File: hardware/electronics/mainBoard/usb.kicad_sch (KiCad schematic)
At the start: 2 parts, among them J1 USB_C_Receptacle_USB2.0, U2 TPS25730D

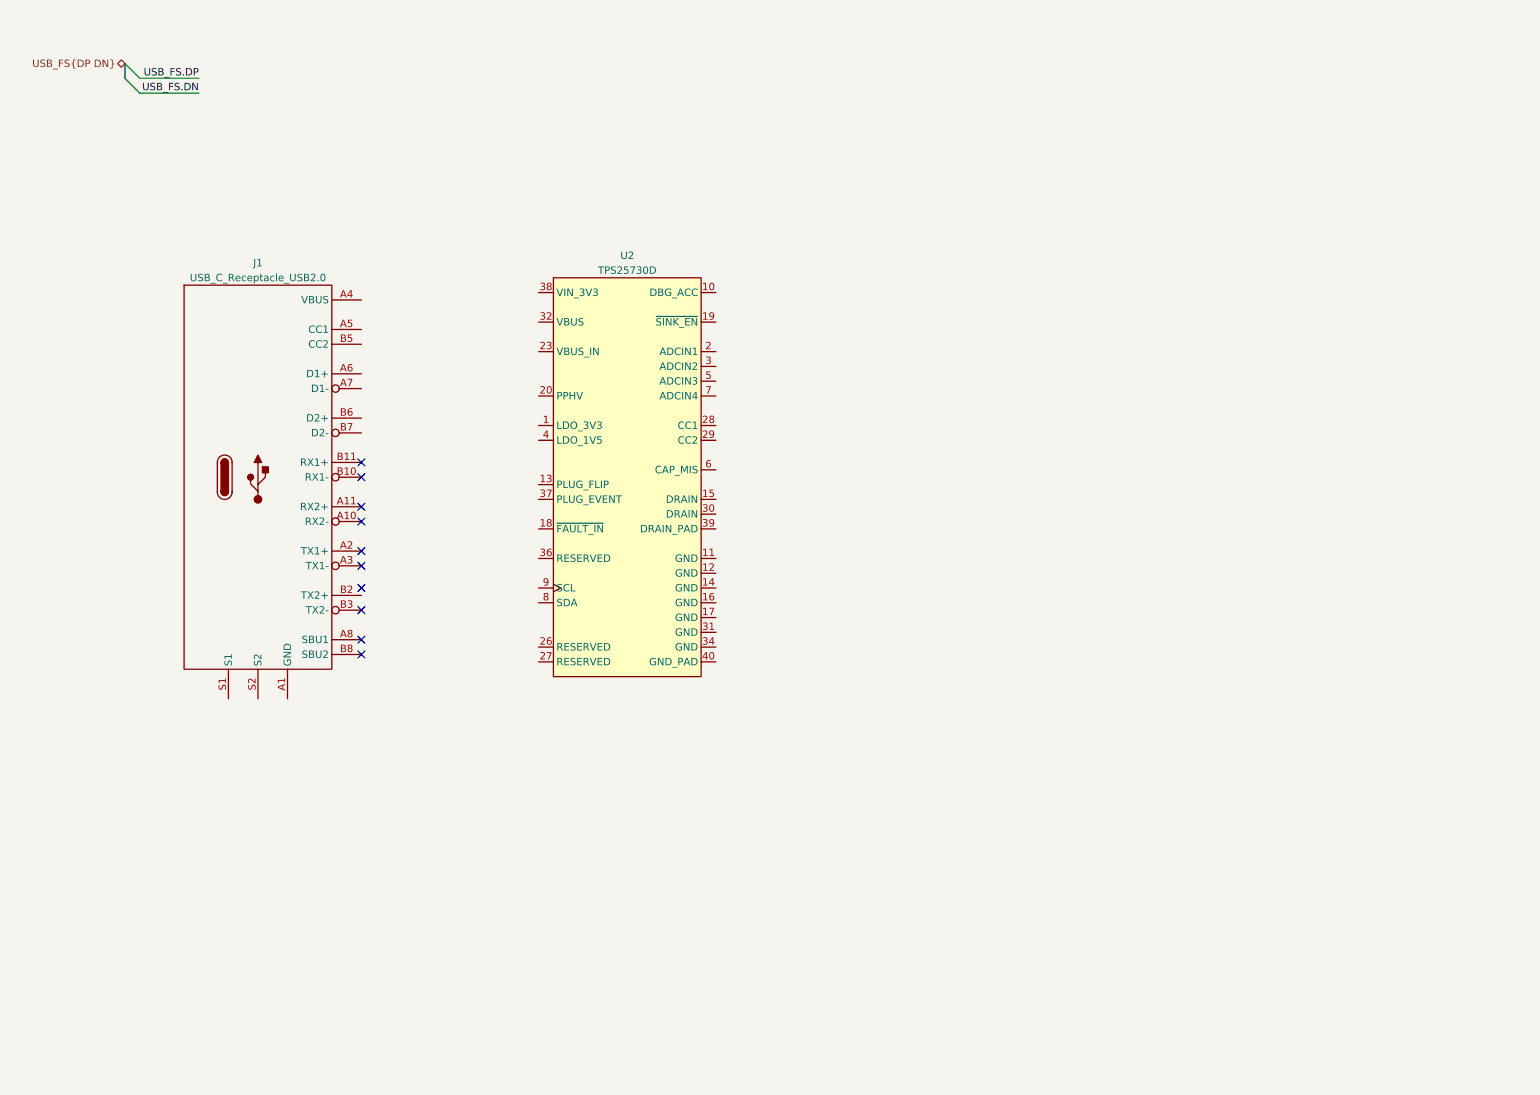
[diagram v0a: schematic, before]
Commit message: added USB PD and Hub circuitry
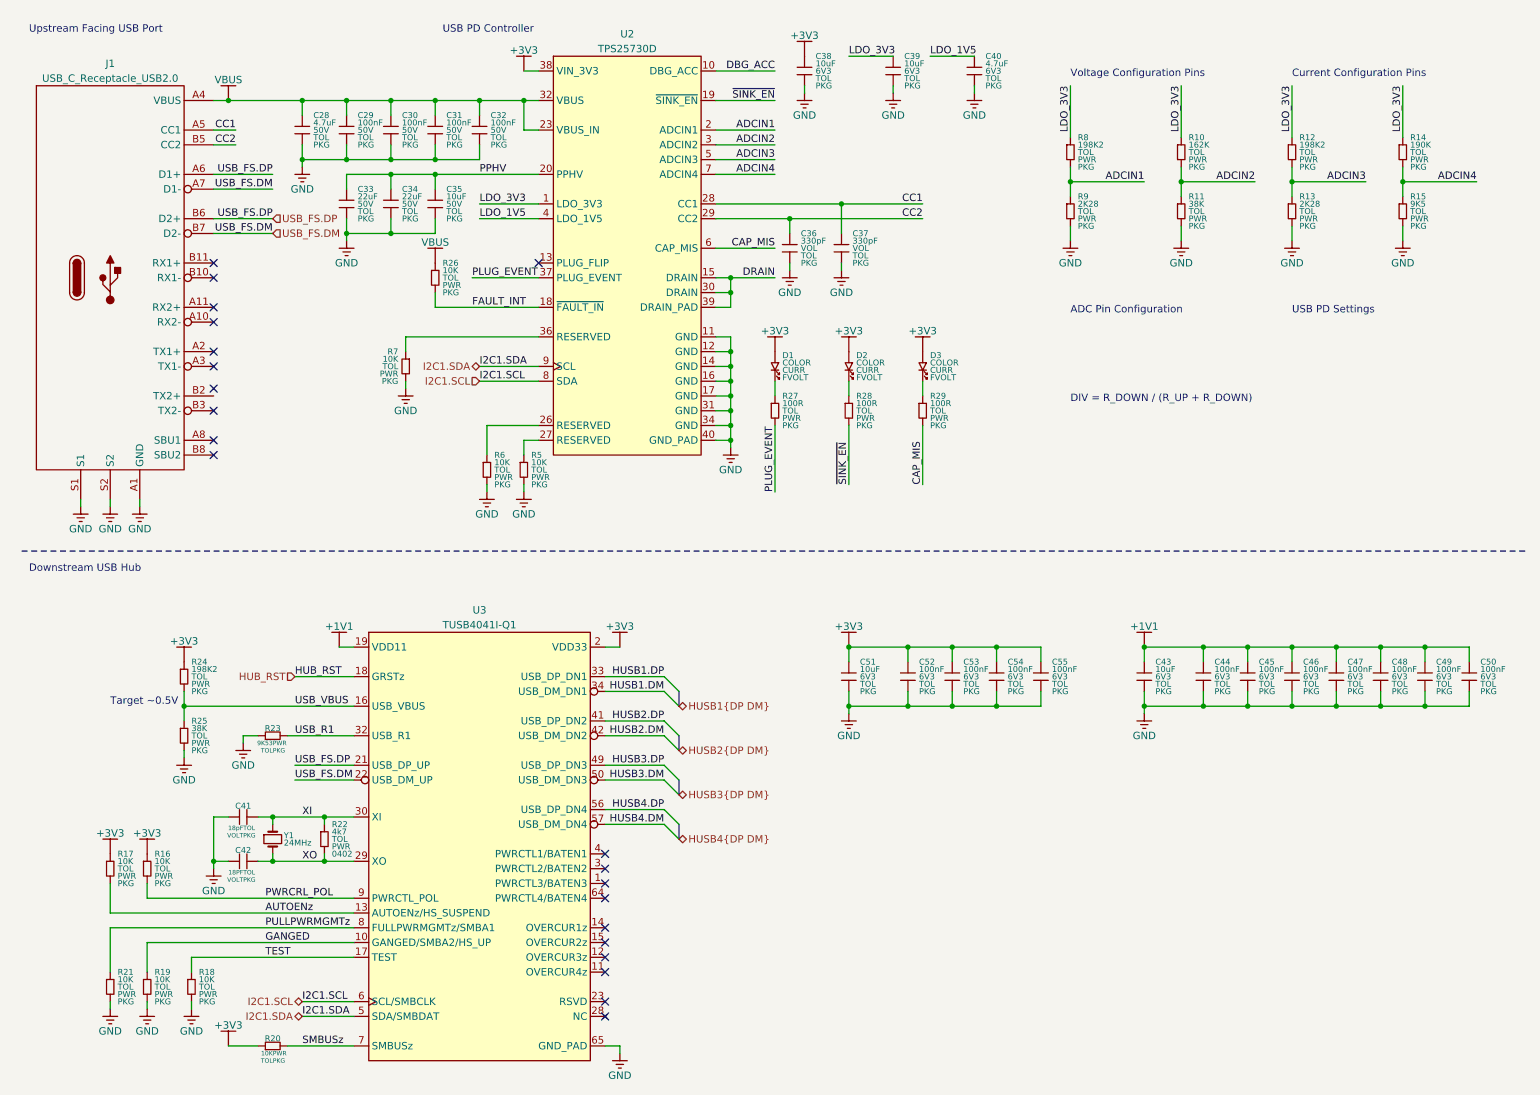
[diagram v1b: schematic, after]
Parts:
- added C28, C40: 4.7uF, symbol .DS-Passives:C
- added C29, C30, C31, C32, C44, C45, C46, C47, C48, C49, C50, C52, C53, C54, C55: 100nF, symbol .DS-Passives:C
- added C33, C34: 22uF, symbol .DS-Passives:C
- added C35, C38, C39, C43, C51: 10uF, symbol .DS-Passives:C
- added C36, C37: 330pF, symbol .DS-Passives:C
- added C41: 18pF, symbol .DS-Passives:C_horizontal
- added C42: 18PF, symbol .DS-Passives:C_horizontal
- added D1, D2, D3: ~, symbol .DS-LEDs:LED
- added R10: 162K, symbol .DS-Passives:R
- added R11, R25: 38K, symbol .DS-Passives:R
- added R12, R24, R8: 198K2, symbol .DS-Passives:R
- added R13, R9: 2K28, symbol .DS-Passives:R
- added R14: 190K, symbol .DS-Passives:R
- added R15: 9K5, symbol .DS-Passives:R
- added R16, R17, R18, R19, R21, R26, R5, R6, R7: 10K, symbol .DS-Passives:R
- added R20: 10K, symbol .DS-Passives:R_horizontal
- added R22: 4k7, symbol .DS-Passives:R
- added R23: 9K53, symbol .DS-Passives:R_horizontal
- added R27, R28, R29: 100R, symbol .DS-Passives:R
- added U3: TUSB4041I-Q1, symbol .DS-ICs:TUSB4041I-Q1
- added Y1: ~, symbol .DS-Crystals-Oscillators-Resonators:crystal_small
- U2: DKPN (none) -> 296-TPS25730DREFRCT-ND; MPN (none) -> TPS25730DREFR
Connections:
- net USB_FS.DP: now also J1.A6 (D1+), J1.B6 (D2+), U3.21 (USB_DP_UP)
- net GND: now reaches J1.A1 (GND), J1.A12 (GND), J1.B1 (GND), J1.B12 (GND)
- net GND: now also J1.S1, J1.S2, U2.11 (GND), U2.12 (GND), U2.14 (GND), U2.16 (GND), U2.17 (GND), U2.31 (GND), U2.34 (GND), U2.35 (GND), U2.40 (GND_PAD), C28.2, C29.2, C30.2, C31.2, C32.2, C33.2, C34.2, C35.2, C36.2, C37.2, C38.2, C39.2, C40.2, C41.1, C42.1, C43.2, C44.2, C45.2, C46.2, C47.2, C48.2, C49.2, C50.2, C51.2, C52.2, C53.2, C54.2, C55.2, R11.2, R13.2, R15.2, R18.2, R19.2, R21.2, R23.1, R25.2, R5.2, R6.2, R7.2, R9.2, U3.65 (GND_PAD)
- net VBUS: now reaches J1.A4 (VBUS), J1.A9 (VBUS), J1.B4 (VBUS), J1.B9 (VBUS)
- net VBUS: now also U2.23 (VBUS_IN), U2.24 (VBUS_IN), U2.25 (VBUS_IN), U2.32 (VBUS), U2.33 (VBUS), C28.1, C29.1, C30.1, C31.1, C32.1, R26.1
- net CC1: now reaches J1.A5 (CC1)
- net CC1: now also U2.28 (CC1), C37.1
- net USB_FS.DM: now reaches J1.A7 (D1-)
- net USB_FS.DM: now also J1.B7 (D2-), U3.22 (USB_DM_UP)
- net CC2: now reaches J1.B5 (CC2)
- net CC2: now also U2.29 (CC2), C36.1
- net LDO_3V3: now reaches U2.1 (LDO_3V3)
- net LDO_3V3: now also C39.1, R10.1, R12.1, R14.1, R8.1
- net DBG_ACC: now reaches U2.10 (DBG_ACC)
- net DRAIN: now reaches U2.15 (DRAIN)
- net DRAIN: now also U2.30 (DRAIN), U2.39 (DRAIN_PAD)
- net FAULT_INT: now reaches U2.18 (~{FAULT_IN})
- net FAULT_INT: now also R26.2
- net ~{SINK_EN}: now reaches U2.19 (~{SINK_EN})
- net ~{SINK_EN}: now also R28.2
- net ADCIN1: now reaches U2.2 (ADCIN1)
- net ADCIN1: now also R8.2, R9.1
- net PPHV: now reaches U2.20 (PPHV), U2.21 (PPHV), U2.22 (PPHV)
- net PPHV: now also C33.1, C34.1, C35.1
- net at U2.26 (RESERVED): now also R6.1
- net at U2.27 (RESERVED): now also R5.1
- net ADCIN2: now reaches U2.3 (ADCIN2)
- net ADCIN2: now also R10.2, R11.1
- net at U2.36 (RESERVED): now also R7.1
- net PLUG_EVENT: now reaches U2.37 (PLUG_EVENT)
- net PLUG_EVENT: now also R27.2
- net +3V3: now reaches U2.38 (VIN_3V3)
- net +3V3: now also C38.1, C51.1, C52.1, C53.1, C54.1, C55.1, D1.1, D2.1, D3.1, R16.1, R17.1, R20.1, R24.1, U3.2 (VDD33), U3.20 (VDD33), U3.31 (VDD33), U3.48 (VDD33)
- net LDO_1V5: now reaches U2.4 (LDO_1V5)
- net LDO_1V5: now also C40.1
- net ADCIN3: now reaches U2.5 (ADCIN3)
- net ADCIN3: now also R12.2, R13.1
- net CAP_MIS: now reaches U2.6 (CAP_MIS)
- net CAP_MIS: now also R29.2
- net ADCIN4: now reaches U2.7 (ADCIN4)
- net ADCIN4: now also R14.2, R15.1
- net I2C1.SCL: now reaches U2.8 (SDA)
- net I2C1.SCL: now also U3.6 (SCL/SMBCLK)
- net I2C1.SDA: now reaches U2.9 (SCL)
- net I2C1.SDA: now also U3.5 (SDA/SMBDAT)
- new net: D2.2, R28.1
- new net: D1.2, R27.1
- new net: D3.2, R29.1
- new net: U3.23 (RSVD), U3.24 (RSVD), U3.26 (RSVD), U3.27 (RSVD), U3.35 (RSVD), U3.36 (RSVD), U3.38 (RSVD), U3.39 (RSVD), U3.43 (RSVD), U3.44 (RSVD), U3.46 (RSVD), U3.47 (RSVD), U3.51 (RSVD), U3.52 (RSVD), U3.54 (RSVD), U3.55 (RSVD), U3.58 (RSVD), U3.59 (RSVD), U3.61 (RSVD), U3.62 (RSVD)
- new net: U3.28 (NC), U3.40 (NC)
- new net +1V1: C43.1, C44.1, C45.1, C46.1, C47.1, C48.1, C49.1, C50.1, U3.19 (VDD11), U3.25 (VDD11), U3.37 (VDD11), U3.45 (VDD11), U3.53 (VDD11), U3.60 (VDD11), U3.63 (VDD11)
- new net AUTOENz: R17.2, U3.13 (AUTOENz/HS_SUSPEND)
- new net GANGED: R19.1, U3.10 (GANGED/SMBA2/HS_UP)
- new net HUB_RST: U3.18 (GRSTz)
- new net HUSB1.DM: U3.34 (USB_DM_DN1)
- new net HUSB1.DP: U3.33 (USB_DP_DN1)
- new net HUSB2.DM: U3.42 (USB_DM_DN2)
- new net HUSB2.DP: U3.41 (USB_DP_DN2)
- new net HUSB3.DM: U3.50 (USB_DM_DN3)
- new net HUSB3.DP: U3.49 (USB_DP_DN3)
- new net HUSB4.DM: U3.57 (USB_DM_DN4)
- new net HUSB4.DP: U3.56 (USB_DP_DN4)
- new net PULLPWRMGMTz: R21.1, U3.8 (FULLPWRMGMTz/SMBA1)
- new net PWRCRL_POL: R16.2, U3.9 (PWRCTL_POL)
- new net SMBUSz: R20.2, U3.7 (SMBUSz)
- new net TEST: R18.1, U3.17 (TEST)
- new net USB_R1: R23.2, U3.32 (USB_R1)
- new net USB_VBUS: R24.2, R25.1, U3.16 (USB_VBUS)
- new net XI: C41.2, R22.1, U3.30 (XI), Y1.1
- new net XO: C42.2, R22.2, U3.29 (XO), Y1.2
- no-connect marks 10 -> 21
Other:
- note added: "ADC Pin Configuration"
- note added: "Current Configuration Pins"
- note added: "DIV = R_DOWN / (R_UP + R_DOWN)"
- note added: "Downstream USB Hub"
- note added: "Target ~0.5V"
- note added: "USB PD Controller"
- note added: "USB PD Settings"
- note added: "Upstream Facing USB Port"
- note added: "Voltage Configuration Pins"
- moved on the sheet: J1, U2

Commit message: usb PD and hub
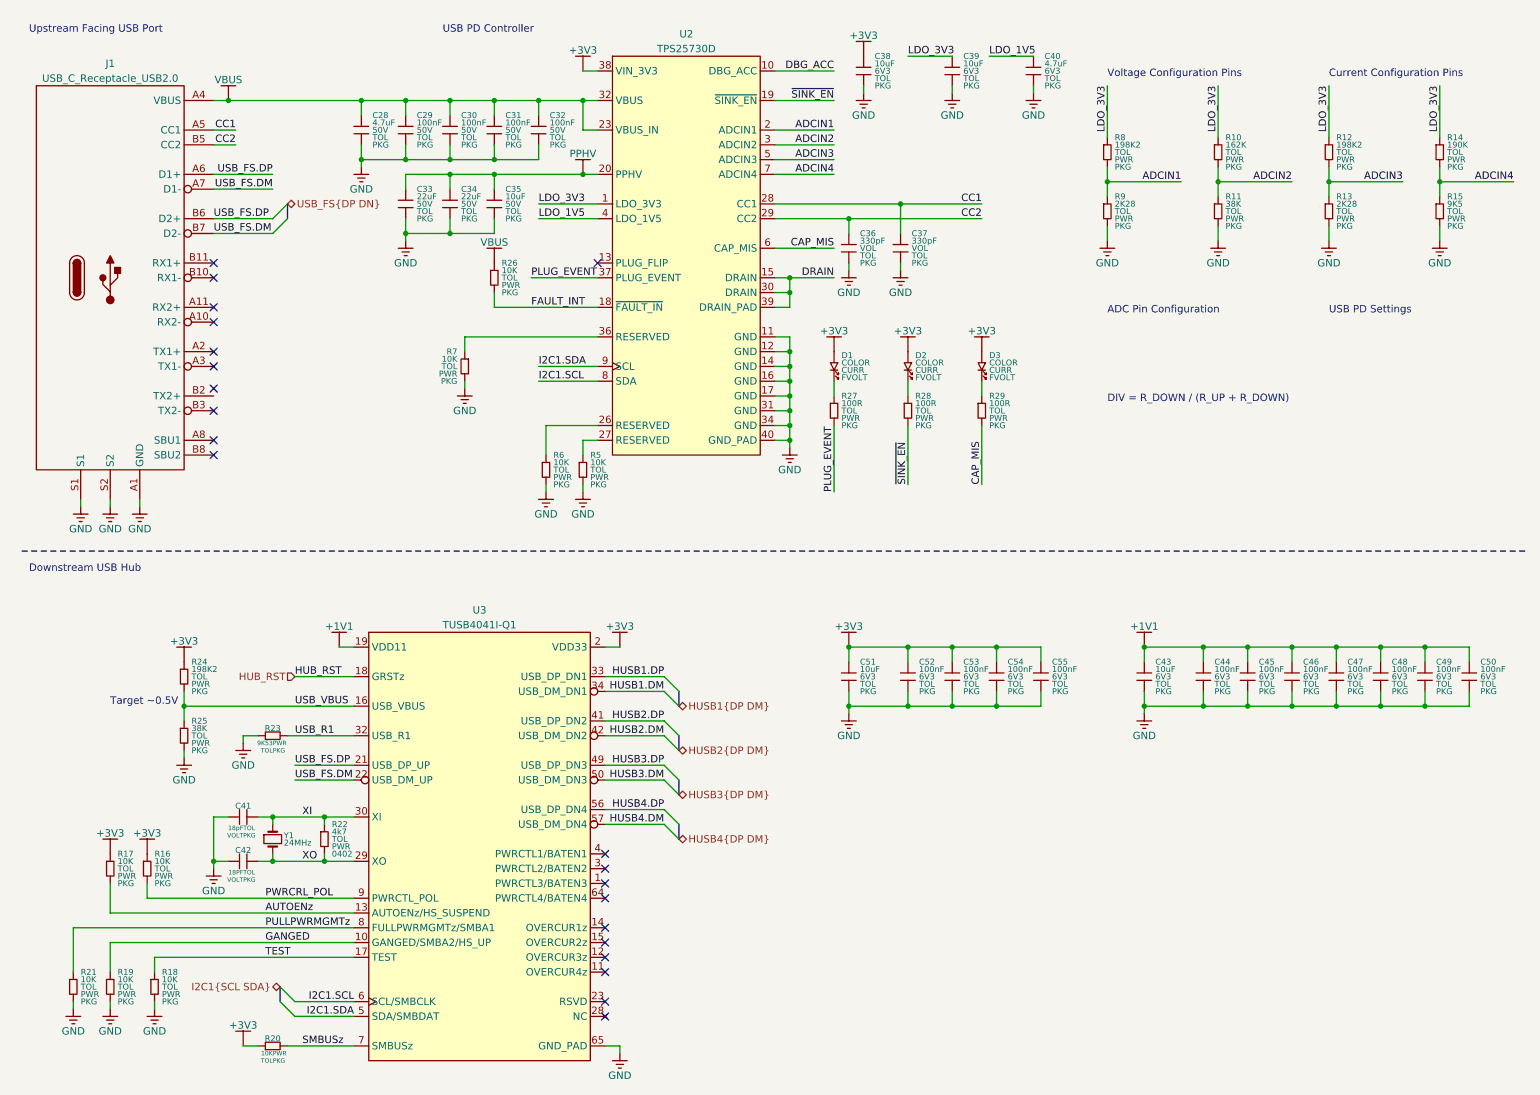
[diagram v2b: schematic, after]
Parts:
- C28, C29, C30, C31, C32, C33, C34, C35, C36, C37, C38, C39, C40, C43, C44, C45, C46, C47, C48, C49, C50, C51, C52, C53, C54, C55: symbol .DS-Passives:C -> lib_sch:C
- C41, C42: symbol .DS-Passives:C_horizontal -> lib_sch:C_horizontal
- D1, D2, D3: symbol .DS-LEDs:LED -> lib_sch:LED
- R10, R11, R12, R13, R14, R15, R16, R17, R18, R19, R21, R22, R24, R25, R26, R27, R28, R29, R5, R6, R7, R8, R9: symbol .DS-Passives:R -> lib_sch:R
- R20, R23: symbol .DS-Passives:R_horizontal -> lib_sch:R_horizontal
- U3: symbol .DS-ICs:TUSB4041I-Q1 -> lib_sch:TUSB4041I-Q1
- Y1: symbol .DS-Crystals-Oscillators-Resonators:crystal_small -> lib_sch:crystal_small
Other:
- moved on the sheet: C28, C29, C30, C31, C32, C33, C34, C35, C36, C37, C38, C39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

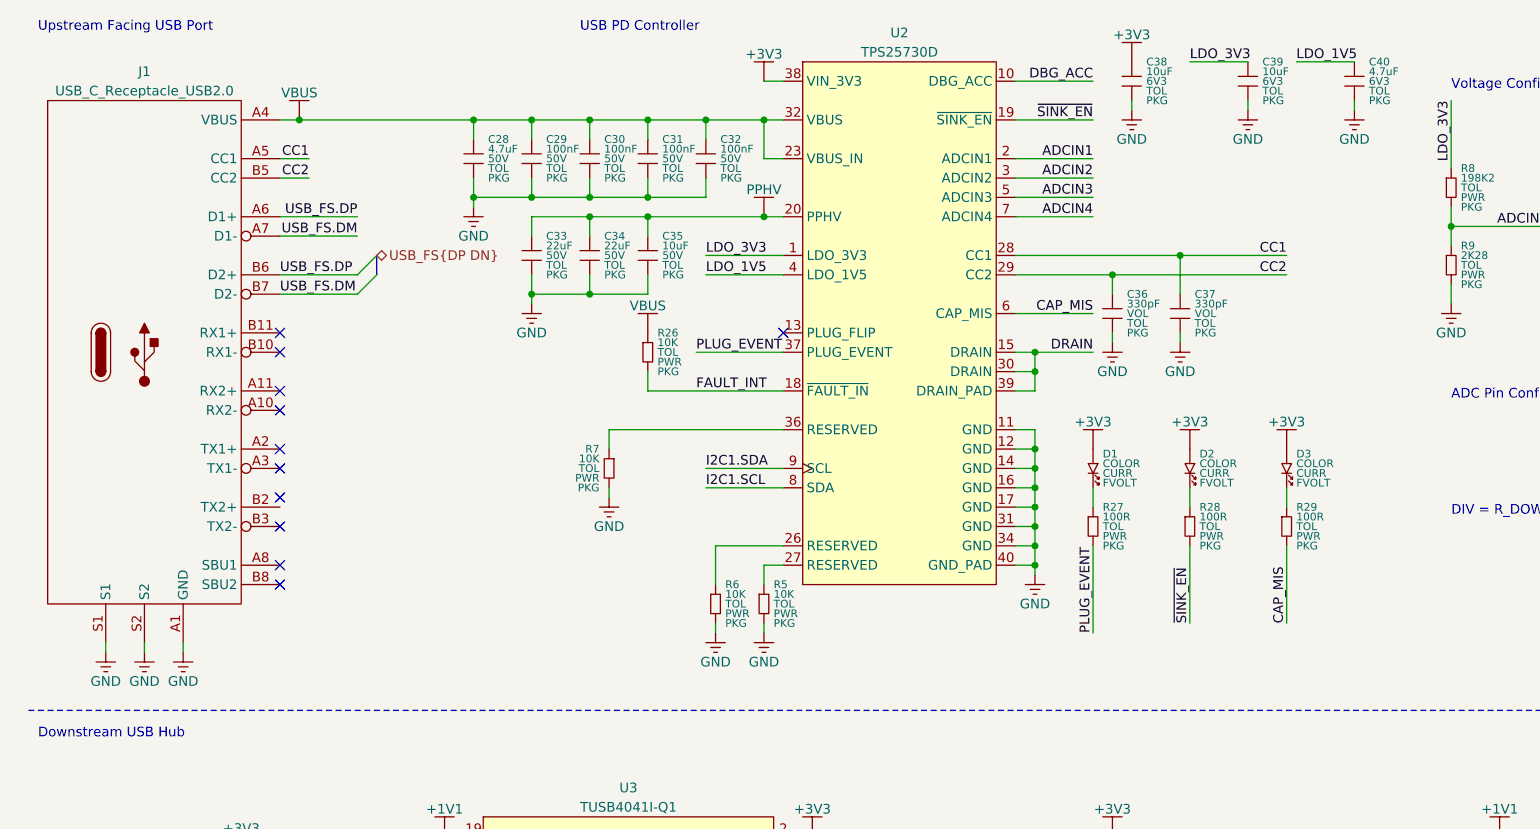
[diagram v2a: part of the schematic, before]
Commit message: replaced PD IC
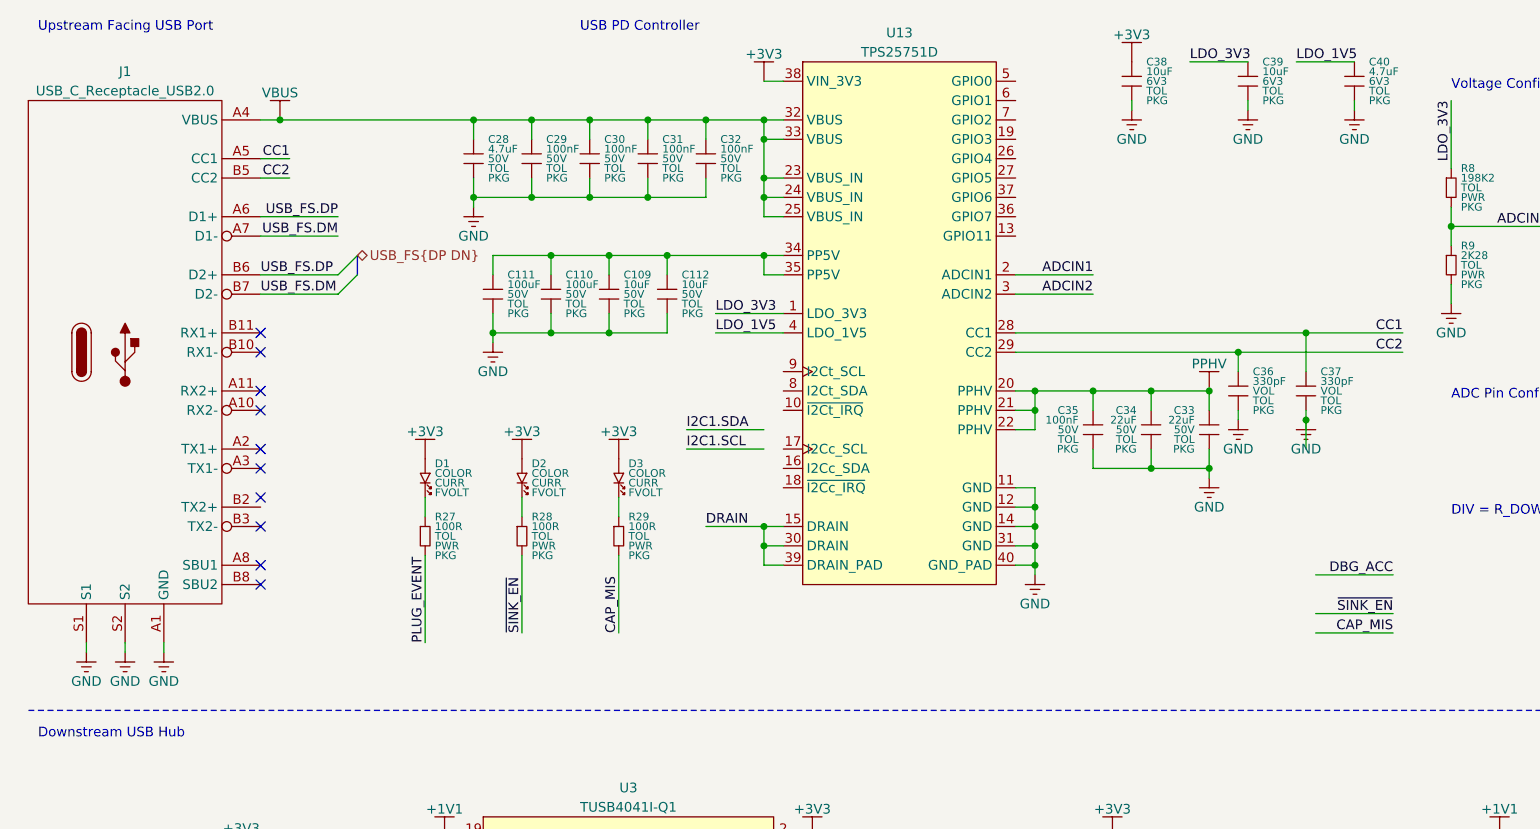
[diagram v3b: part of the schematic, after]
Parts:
- removed R26, R5, R6, R7: 10K, symbol lib_sch:R
- removed U2: TPS25730D, symbol lib_sch:TPS25730D
- added C109, C112: 10uF, symbol lib_sch:C
- added C110, C111: 100uF, symbol lib_sch:C
- added U13: TPS25751D, symbol .DS-PMIC:TPS25751D
- C35: value 10uF -> 100nF
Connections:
- net +3V3: now also U13.38 (VIN_3V3)
- net ADCIN1: now also U13.2 (ADCIN1)
- net ADCIN2: now also U13.3 (ADCIN2)
- net CC1: now also U13.28 (CC1)
- net CC2: now also U13.29 (CC2)
- net DRAIN: now also U13.15 (DRAIN), U13.30 (DRAIN), U13.39 (DRAIN_PAD)
- net GND: now also C109.2, C110.2, C111.2, C112.2, U13.11 (GND), U13.12 (GND), U13.14 (GND), U13.31 (GND), U13.40 (GND_PAD)
- net LDO_1V5: now also U13.4 (LDO_1V5)
- net LDO_3V3: now also U13.1 (LDO_3V3)
- net PPHV: now also U13.20 (PPHV), U13.21 (PPHV), U13.22 (PPHV)
- net VBUS: now also U13.23 (VBUS_IN), U13.24 (VBUS_IN), U13.25 (VBUS_IN), U13.32 (VBUS), U13.33 (VBUS)
- new net: C109.1, C110.1, C111.1, C112.1, U13.34 (PP5V), U13.35 (PP5V)
- no-connect marks 21 -> 20
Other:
- moved on the sheet: C33, C34, C35, C36, C37, D1, D2, D3, J1, R27, R28, R29
